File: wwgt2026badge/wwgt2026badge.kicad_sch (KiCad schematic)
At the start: 16 parts, among them J1 Conn_01x08_Pin, J2 Conn_01x04_Pin, SW1 SW_PUSH, SW2 EC12PLGRSDVF, SW3 SW_PUSH, U2 rp2040-zero, U3 fj08k-s

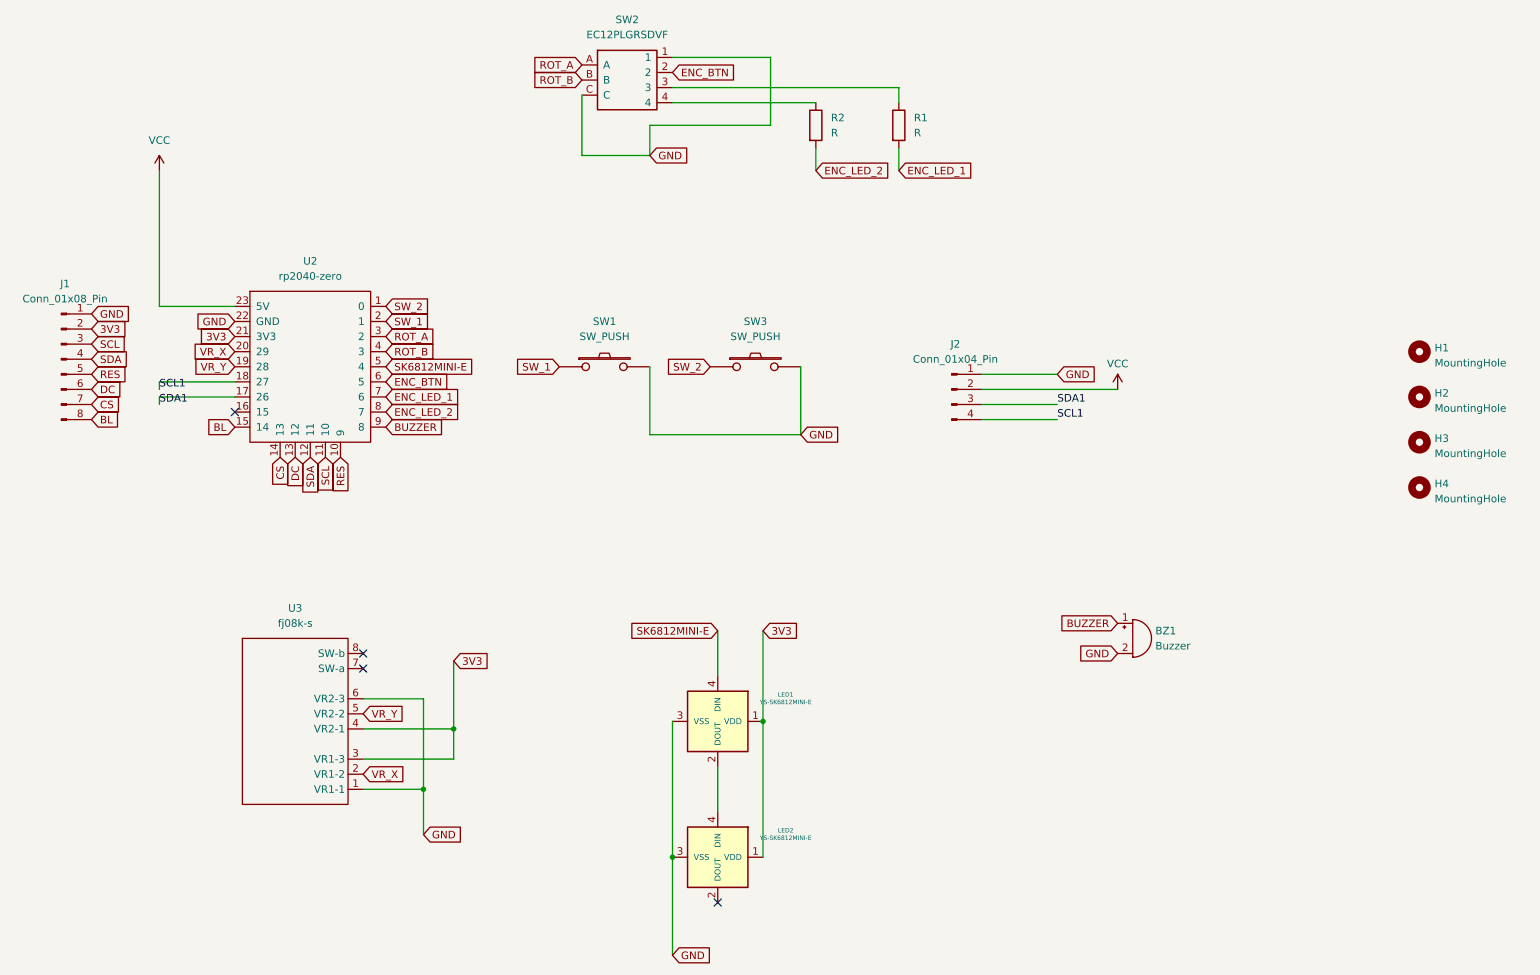
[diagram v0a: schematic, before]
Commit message: エンコーダーのフットプリントを修正 + 回路およびPCBのエラーを修正
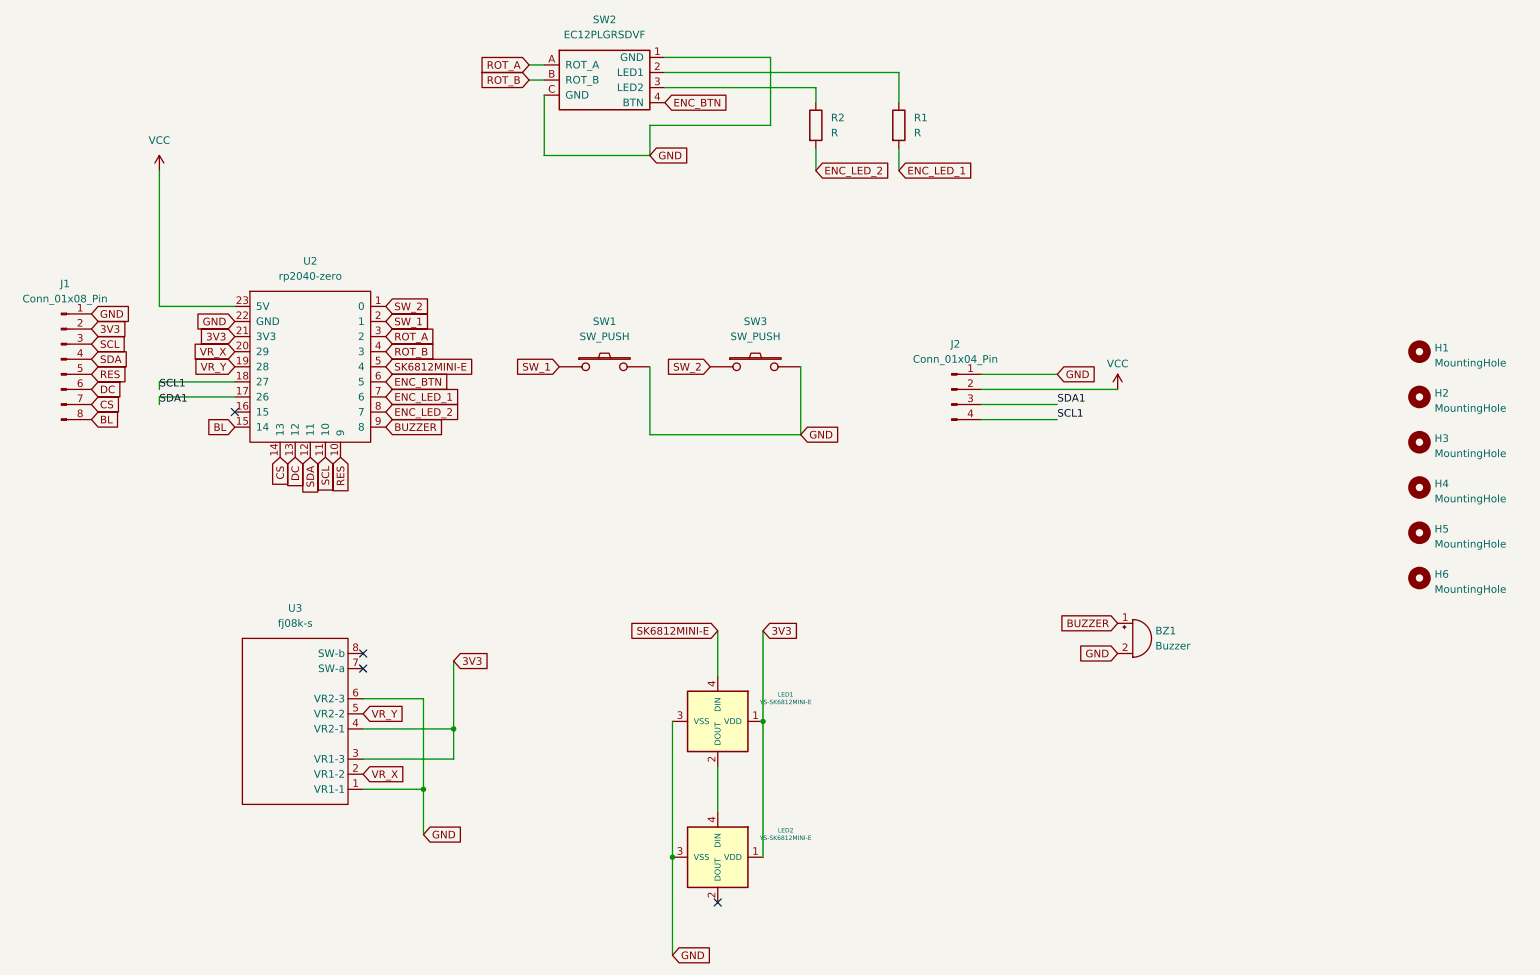
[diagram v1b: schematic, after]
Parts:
- added H5, H6: MountingHole, foostan/kbd:M2_HOLE_v2, symbol Mechanical:MountingHole
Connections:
- net ENC_BTN: now also SW2.4 (BTN); no longer SW2.2
- net at R1.1: now also SW2.2 (LED1); no longer SW2.3
- net at R2.1: now also SW2.3 (LED2); no longer SW2.4
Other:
- moved on the sheet: SW2
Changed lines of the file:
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@@
 	(wire
 		(pts
-			(xy 163.83 41.91) (xy 163.83 44.45)
+			(xy 163.83 39.37) (xy 163.83 44.45)
 		)
 		(stroke
@@
 	(wire
 		(pts
-			(xy 125.73 36.83) (xy 142.24 36.83)
+			(xy 101.6 38.1) (xy 104.14 38.1)
+		)
+		(stroke
+			(width 0)
+			(type default)
+		)
+	)
+	(wire
+		(pts
+			(xy 124.46 39.37) (xy 163.83 39.37)
 		)
 		(stroke
@@
 	(wire
 		(pts
-			(xy 110.49 53.34) (xy 121.92 53.34)
+			(xy 104.14 53.34) (xy 121.92 53.34)
 		)
 		(stroke
@@
 	(wire
 		(pts
+			(xy 149.86 41.91) (xy 149.86 44.45)
+		)
+		(stroke
+			(width 0)
+			(type default)
+		)
+	)
+	(wire
+		(pts
 			(xy 52.07 91.44) (xy 39.37 91.44)
 		)
@@
 	(wire
 		(pts
-			(xy 125.73 41.91) (xy 163.83 41.91)
+			(xy 124.46 36.83) (xy 142.24 36.83)
 		)
 		(stroke
@@
 	(wire
 		(pts
+			(xy 124.46 41.91) (xy 149.86 41.91)
+		)
+		(stroke
+			(width 0)
+			(type default)
+		)
+	)
+	(wire
+		(pts
 			(xy 39.37 78.74) (xy 52.07 78.74)
 		)
@@
 	(wire
 		(pts
-			(xy 110.49 43.18) (xy 110.49 53.34)
-		)
-		(stroke
-			(width 0)
-			(type default)
-		)
-	)
-	(wire
-		(pts
-			(xy 125.73 44.45) (xy 149.86 44.45)
+			(xy 104.14 43.18) (xy 104.14 53.34)
+		)
+		(stroke
+			(width 0)
+			(type default)
+		)
+	)
+	(wire
+		(pts
+			(xy 101.6 40.64) (xy 104.14 40.64)
 		)
 		(stroke
@@
 	(global_label "ROT_B"
 		(shape input)
-		(at 110.49 40.64 180)
+		(at 101.6 40.64 180)
 		(fields_autoplaced yes)
 		(effects
@@
 		)
 		(property "Intersheetrefs" "${INTERSHEET_REFS}"
-			(at 101.6991 40.64 0)
+			(at 92.8091 40.64 0)
 			(effects
 				(font
@@
 	(global_label "ROT_A"
 		(shape input)
-		(at 110.49 38.1 180)
+		(at 101.6 38.1 180)
 		(fields_autoplaced yes)
 		(effects
@@
 		)
 		(property "Intersheetrefs" "${INTERSHEET_REFS}"
-			(at 101.8805 38.1 0)
+			(at 92.9905 38.1 0)
 			(effects
 				(font
@@
 	(global_label "ENC_BTN"
 		(shape input)
-		(at 125.73 39.37 0)
-		(fields_autoplaced yes)
-		(effects
-			(font
-				(size 1.27 1.27)
-			)
-			(justify left)
-		)
-		(property "Intersheetrefs" "${INTERSHEET_REFS}"
-			(at 137.0004 39.37 0)
+		(at 124.46 44.45 0)
+		(fields_autoplaced yes)
+		(effects
+			(font
+				(size 1.27 1.27)
+			)
+			(justify left)
+		)
+		(property "Intersheetrefs" "${INTERSHEET_REFS}"
+			(at 135.7304 44.45 0)
 			(effects
 				(font
@@
 	)
 	(symbol
-		(lib_id "ALPS_EC12PLGRSDVF_D_25K_24_24C_31_07_6H:ALPS_EC12PLGRSDVF_D_25K_24_24C_31_07_6H")
-		(at 118.11 40.64 0)
+		(lib_id "Mechanical:MountingHole")
+		(at 251.46 124.46 0)
 		(unit 1)
 		(exclude_from_sim no)
@@
 		(dnp no)
 		(fields_autoplaced yes)
+		(property "Reference" "H6"
+			(at 254 123.825 0)
+			(effects
+				(font
+					(size 1.27 1.27)
+				)
+				(justify left)
+			)
+		)
+		(property "Value" "MountingHole"
+			(at 254 126.365 0)
+			(effects
+				(font
+					(size 1.27 1.27)
+				)
+				(justify left)
+			)
+		)
+		(property "Footprint" "foostan/kbd:M2_HOLE_v2"
+			(at 251.46 124.46 0)
+			(effects
+				(font
+					(size 1.27 1.27)
+				)
+				(hide yes)
+			)
+		)
+		(property "Datasheet" "~"
+			(at 251.46 124.46 0)
+			(effects
+				(font
+					(size 1.27 1.27)
+				)
+				(hide yes)
+			)
+		)
+		(property "Description" ""
+			(at 251.46 124.46 0)
+			(effects
+				(font
+					(size 1.27 1.27)
+				)
+			)
+		)
+		(instances
+			(project "wwgt2026badge"
+				(path "/4597c5c7-ab98-46a0-a1d3-ac8e59abbe7d"
+					(reference "H6")
+					(unit 1)
+				)
+			)
+		)
+	)
+	(symbol
+		(lib_id "ALPS_EC12PLGRSDVF_D_25K_24_24C_31_07_6H:ALPS_EC12PLGRSDVF_D_25K_24_24C_31_07_6H")
+		(at 114.3 40.64 0)
+		(unit 1)
+		(exclude_from_sim no)
+		(in_bom yes)
+		(on_board yes)
+		(dnp no)
+		(fields_autoplaced yes)
 		(property "Reference" "SW2"
-			(at 118.11 30.48 0)
+			(at 114.3 30.48 0)
 			(effects
 				(font
@@
 		)
 		(property "Value" "EC12PLGRSDVF"
-			(at 118.11 33.02 0)
+			(at 114.3 33.02 0)
 			(effects
 				(font
@@
 		)
 		(property "Footprint" "sglib:RotaryEncoder_Alps_EC12E-Switch_Vertical_H20mm_LED"
-			(at 118.11 50.8 0)
+			(at 114.3 50.8 0)
 			(effects
 				(font
@@
 		)
 		(property "Datasheet" ""
-			(at 118.11 53.34 0)
+			(at 114.3 53.34 0)
 			(effects
 				(font
@@
 		)
 		(property "Description" ""
-			(at 118.11 40.64 0)
+			(at 114.3 40.64 0)
 			(effects
 				(font
@@
 					(unit 1)
 				)
+			)
+		)
+	)
+	(symbol
+		(lib_id "Mechanical:MountingHole")
+		(at 251.46 116.84 0)
+		(unit 1)
+		(exclude_from_sim no)
+		(in_bom yes)
+		(on_board yes)
+		(dnp no)
+		(fields_autoplaced yes)
+		(property "Reference" "H5"
+			(at 254 116.205 0)
+			(effects
+				(font
+					(size 1.27 1.27)
+				)
+				(justify left)
+			)
+		)
+		(property "Value" "MountingHole"
+			(at 254 118.745 0)
+			(effects
+				(font
+					(size 1.27 1.27)
+				)
+				(justify left)
+			)
+		)
+		(property "Footprint" "foostan/kbd:M2_HOLE_v2"
+			(at 251.46 116.84 0)
+			(effects
+				(font
+					(size 1.27 1.27)
+				)
+				(hide yes)
+			)
+		)
+		(property "Datasheet" "~"
+			(at 251.46 116.84 0)
+			(effects
+				(font
+					(size 1.27 1.27)
+				)
+				(hide yes)
+			)
+		)
+		(property "Description" ""
+			(at 251.46 116.84 0)
+			(effects
+				(font
+					(size 1.27 1.27)
+				)
+			)
+		)
+		(instances
+			(project "wwgt2026badge"
+				(path "/4597c5c7-ab98-46a0-a1d3-ac8e59abbe7d"
+					(reference "H5")
+					(unit 1)
+				)
